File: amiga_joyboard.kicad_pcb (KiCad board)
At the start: 2 copper layers, 18 parts, among them J1 JOYPORT_OUT, SW1 FIRE_BTN, SW2 B_BTN, SW3 A_BTN, SW4 RIGHT_BTN, SW5 LEFT_BTN, SW6 DOWN_BTN, SW7 UP_BTN, SW8 AUTOFIRE_SW, SW9 AMIGA_C64_SW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

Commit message: boards separated
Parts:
- added J2: CONN_D, Connector_JST:JST_XH_S5B-XH-A_1x05_P2.50mm_Horizontal, F.Cu at (88.0, 50.5)
- added J3: CONN_F, Connector_JST:JST_XH_S5B-XH-A_1x05_P2.50mm_Horizontal, F.Cu at (173.6, 50.5)
- moved SW9 33.4 mm to (180.9, 57.2), turned to 0 degrees
- moved R1 25.2 mm to (177.8, 73.5)
- moved C2 9.86 mm to (154.9, 55.1)
- moved J1 9.36 mm to (69.5, 50.5)
- moved U1 8.39 mm to (159.3, 61.3)
- moved R3 8.27 mm to (179.1, 67.1)
- moved C1 7.84 mm to (172.7, 67.6)
- moved RV1 7.74 mm to (195.6, 67.8)
- moved R2 7.31 mm to (186.7, 63.3)
- moved D1 5.88 mm to (149.4, 59.5)
- moved SW8 5.63 mm to (145.6, 68.1)
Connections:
- C1 pad 2: GND -> GND_F
- C2 pad 2: GND -> GND_F
- J1 pad 5: /B -> /B_D
- J1 pad 6: /FIRE -> /FIRE_D
- J1 pad 7: VCC -> VCC_D
- J1 pad 8: GND -> GND_D
- J1 pad 9: /A -> /A_D
- R2 pad 2: VCC -> VCC_F
- SW1 pad 1: /FIRE -> /FIRE_F
- SW2 pad 1: /B -> /B_F
- SW3 pad 1: /A -> /A_F
- SW4 pad 2: GND -> GND_D
- SW5 pad 2: GND -> GND_D
- SW6 pad 2: GND -> GND_D
- SW7 pad 2: GND -> GND_D
- SW8 pad 2: GND -> GND_F
- SW9 pad 2: GND -> GND_F
- SW9 pad 3: VCC -> VCC_F
- U1 pad 1: GND -> GND_F
- U1 pad 4: VCC -> VCC_F
- U1 pad 8: VCC -> VCC_F

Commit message: first complete design
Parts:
- added REF**: MountingHole_M3, MountingHole:MountingHole_3.2mm_M3_ISO7380_Pad, F.Cu at (58.4, 75.4)
- added REF**: MountingHole_M3, MountingHole:MountingHole_3.2mm_M3_ISO7380_Pad, F.Cu at (121.9, 101.6)
- added REF**: MountingHole_M3, MountingHole:MountingHole_3.2mm_M3_ISO7380_Pad, F.Cu at (121.9, 75.4)
- added REF**: MountingHole_M3, MountingHole:MountingHole_3.2mm_M3_ISO7380_Pad, F.Cu at (231.1, 75.4)
- added REF**: MountingHole_M3, MountingHole:MountingHole_3.2mm_M3_ISO7380_Pad, F.Cu at (58.4, 101.6)
- added REF**: MountingHole_M3, MountingHole:MountingHole_3.2mm_M3_ISO7380_Pad, F.Cu at (170.2, 75.4)
- added REF**: MountingHole_M3, MountingHole:MountingHole_3.2mm_M3_ISO7380_Pad, F.Cu at (165.4, 101.6)
- R1: value 270 -> 100
- moved RV1 51.9 mm to (238.8, 96.4)
- moved SW2 50.1 mm to (223.8, 118.6)
- moved R3 48.3 mm to (212.3, 102.1)
- moved D1 47.6 mm to (184.4, 91.8)
- moved SW8 47.6 mm to (180.6, 100.3)
- moved R2 47.5 mm to (220.0, 97.3)
- moved R1 47.4 mm to (211.1, 107.2)
- moved C2 46.3 mm to (188.2, 87.3)
- moved SW9 46.3 mm to (214.2, 89.5)
- moved U1 46.3 mm to (192.5, 93.6)
- moved C1 46.3 mm to (206.0, 99.9)
- moved SW3 46.3 mm to (200.9, 118.6)
- moved J3 46.3 mm to (206.9, 82.8)
- moved SW1 42.8 mm to (178.1, 118.6)
- moved SW4 41.5 mm to (112.5, 118.6)
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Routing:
- net /A_F: track 0.00 -> 82.5 mm
- net /FIRE_F: track 0.00 -> 75.5 mm
- net Net-(U1-THR): track 0.00 -> 65.9 mm, vias 0 -> 2
- net /RIGHT: track 0.00 -> 57.9 mm
- net VCC_F: track 0.00 -> 57.4 mm, vias 0 -> 2
- net /B_F: track 0.00 -> 49.6 mm, vias 0 -> 2
- net Net-(R1-Pad1): track 0.00 -> 46.2 mm
- net /DOWN: track 0.00 -> 44.8 mm
- net /A_D: track 0.00 -> 43.8 mm
- net /LEFT: track 0.00 -> 42.6 mm
- net /FIRE_D: track 0.00 -> 36.1 mm, vias 0 -> 2
- net /AUTOFIRE: track 0.00 -> 34.6 mm, vias 0 -> 2
- net VCC_D: track 0.00 -> 32.3 mm, vias 0 -> 2
- net Net-(SW9-B): track 0.00 -> 31.1 mm, vias 0 -> 2
- net /B_D: track 0.00 -> 30.3 mm, vias 0 -> 2
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- added copper zone on B.Cu, net GND_D
- added copper zone on B.Cu, net GND_F
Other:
- board outline added: 192.5 x 63.5 mm

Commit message: fill tweaks
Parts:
- moved REF** 0.51 mm to (164.8, 101.6)
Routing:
- net GND_D: track 25.3 -> 60.3 mm
- net GND_F: track 22.6 -> 25.9 mm
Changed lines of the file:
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@@
 	(footprint "MountingHole:MountingHole_3.2mm_M3_ISO7380_Pad"
 		(layer "F.Cu")
-		(at 165.354 101.6)
+		(at 164.846 101.6)
 		(descr "Mounting Hole 3.2mm, M3, ISO7380")
 		(tags "mounting hole 3.2mm m3 iso7380")
@@
 	)
 	(segment
+		(start 215.138 91.52)
+		(end 215.138 91.948)
+		(width 1)
+		(layer "B.Cu")
+		(net 2)
+	)
+	(segment
 		(start 190.221113 82.804)
 		(end 196.89 82.804)
@@
 	)
 	(segment
+		(start 217.17 89.488)
+		(end 215.138 91.52)
+		(width 1)
+		(layer "B.Cu")
+		(net 2)
+	)
+	(segment
 		(start 189.738 91.44)
 		(end 189.738 95.452)
@@
 	)
 	(segment
+		(start 94.343497 71.229497)
+		(end 94.343497 73.261497)
+		(width 1)
+		(layer "B.Cu")
+		(net 9)
+	)
+	(segment
 		(start 108.712 116.078)
 		(end 106.934 114.3)
@@
 	)
 	(segment
+		(start 79.077 69.98)
+		(end 93.094 69.98)
+		(width 1)
+		(layer "B.Cu")
+		(net 9)
+	)
+	(segment
+		(start 73.058 77.724)
+		(end 73.058 75.999)
+		(width 1)
+		(layer "B.Cu")
+		(net 9)
+	)
+	(segment
+		(start 95.758 74.676)
+		(end 95.758 74.93)
+		(width 1)
+		(layer "B.Cu")
+		(net 9)
+	)
+	(segment
+		(start 73.058 77.724)
+		(end 73.058 80.17)
+		(width 1)
+		(layer "B.Cu")
+		(net 9)
+	)
+	(segment
 		(start 82.55 104.648)
 		(end 82.826675 104.924675)
@@
 	)
 	(segment
+		(start 99.06 77.724)
+		(end 96.774 77.724)
+		(width 1)
+		(layer "B.Cu")
+		(net 9)
+	)
+	(segment
+		(start 93.094 69.98)
+		(end 93.472 70.358)
+		(width 1)
+		(layer "B.Cu")
+		(net 9)
+	)
+	(segment
 		(start 62.992 116.078)
 		(end 60.96 114.046)
+		(width 1)
+		(layer "B.Cu")
+		(net 9)
+	)
+	(segment
+		(start 93.472 70.358)
+		(end 94.343497 71.229497)
+		(width 1)
+		(layer "B.Cu")
+		(net 9)
+	)
+	(segment
+		(start 94.343497 73.261497)
+		(end 94.996 73.914)
+		(width 1)
+		(layer "B.Cu")
+		(net 9)
+	)
+	(segment
+		(start 94.996 73.914)
+		(end 95.758 74.676)
+		(width 1)
+		(layer "B.Cu")
+		(net 9)
+	)
+	(segment
+		(start 73.058 75.999)
+		(end 79.077 69.98)
 		(width 1)
 		(layer "B.Cu")
@@
 		(priority 1)
 		(connect_pads
-			(clearance 0.5)
-		)
-		(min_thickness 0.25)
+			(clearance 1)
+		)
+		(min_thickness 0.7)
 		(filled_areas_thickness no)
 		(fill yes
-			(thermal_gap 0.5)
-			(thermal_bridge_width 0.5)
+			(thermal_gap 0.7)
+			(thermal_bridge_width 0.7)
 			(smoothing fillet)
-			(radius 0.5)
+			(radius 2)
 		)
 		(polygon
@@
 		(hatch edge 0.5)
 		(connect_pads
-			(clearance 0.5)
-		)
-		(min_thickness 0.25)
+			(clearance 1)
+		)
+		(min_thickness 0.7)
 		(filled_areas_thickness no)
 		(fill yes
-			(thermal_gap 0.5)
-			(thermal_bridge_width 0.5)
+			(thermal_gap 0.7)
+			(thermal_bridge_width 0.7)
 			(smoothing fillet)
-			(radius 0.5)
+			(radius 2)
 		)
 		(polygon

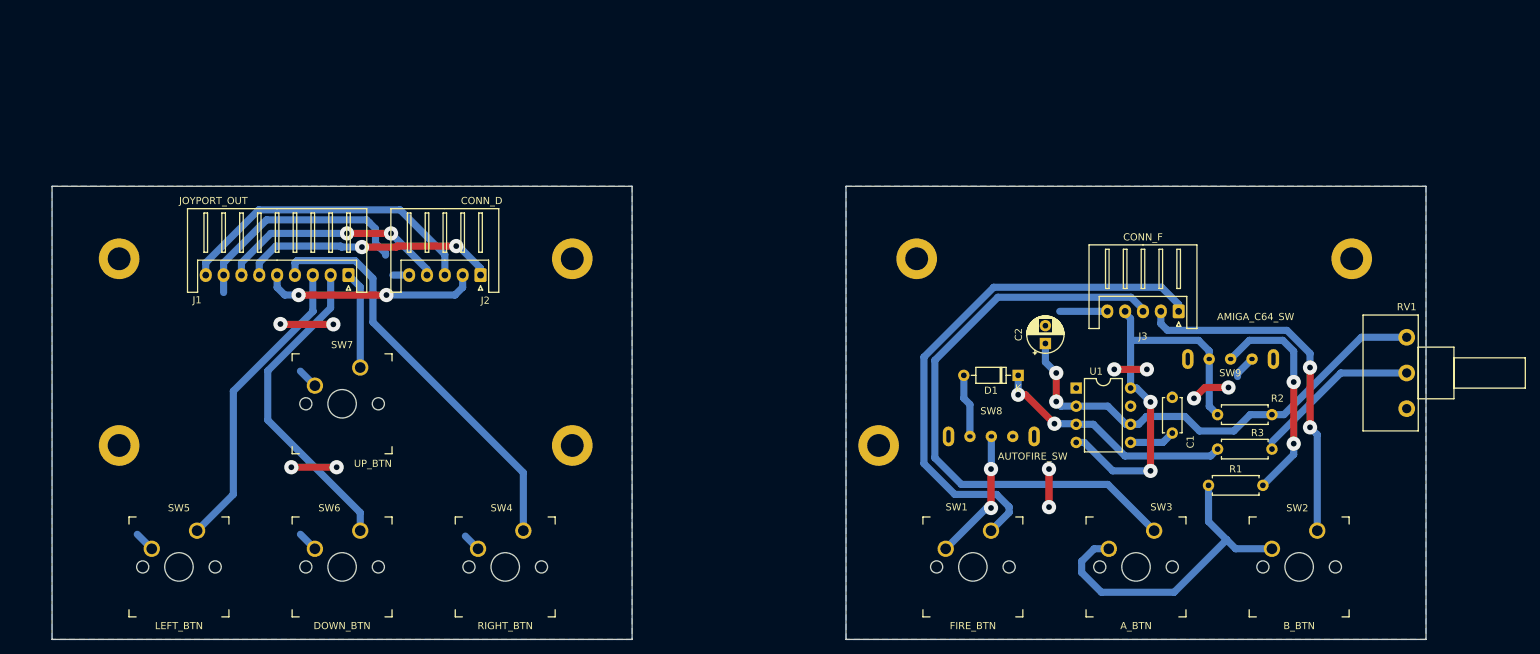
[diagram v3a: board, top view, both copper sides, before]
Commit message: m3 mounting holes swapped for m5 holes (to accommodate a post with m3 screw going through)
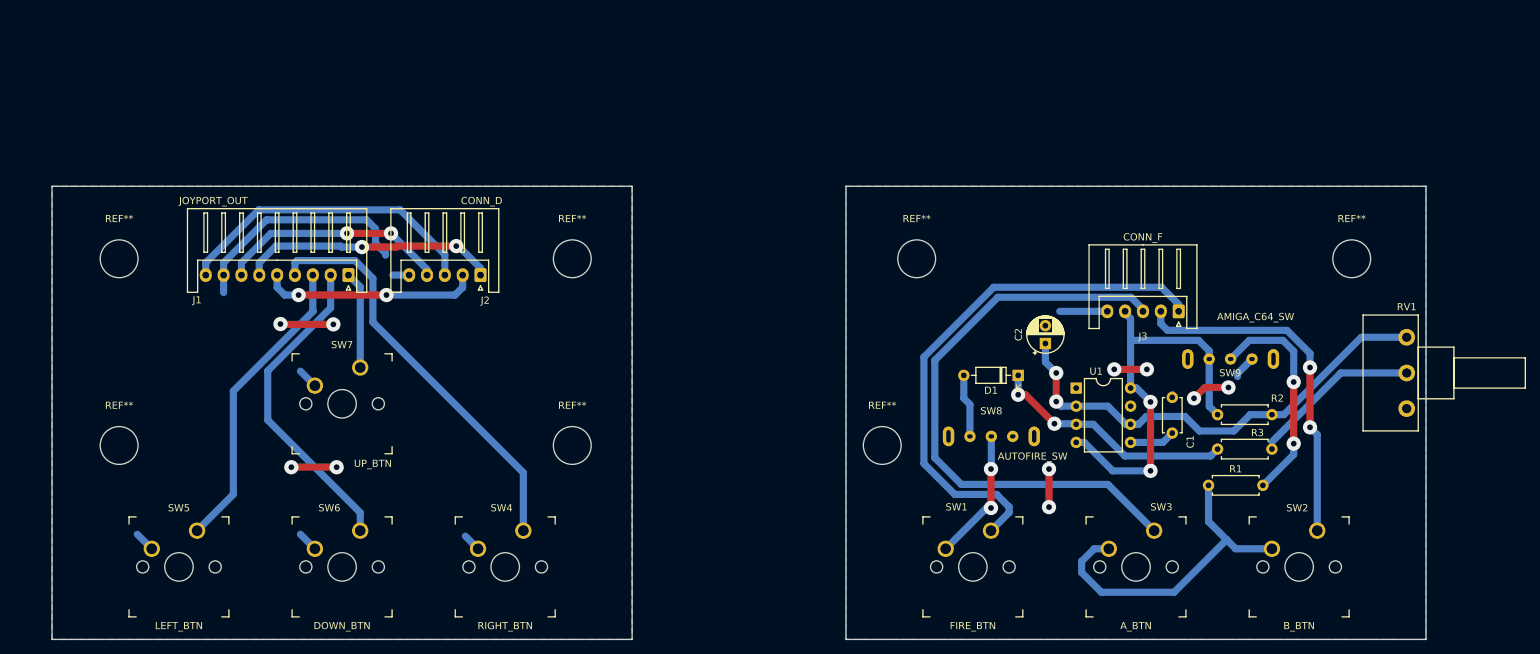
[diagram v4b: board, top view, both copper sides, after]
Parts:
- REF** (x7): footprint MountingHole:MountingHole_3.2mm_M3_ISO7380_Pad -> MountingHole:MountingHole_5.3mm_M5_DIN965
- moved REF** 0.51 mm to (165.4, 101.6)
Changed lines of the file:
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@@
 		)
 	)
-	(footprint "MountingHole:MountingHole_3.2mm_M3_ISO7380_Pad"
+	(footprint "MountingHole:MountingHole_5.3mm_M5_DIN965"
 		(layer "F.Cu")
 		(at 58.42 75.438)
-		(descr "Mounting Hole 3.2mm, M3, ISO7380")
-		(tags "mounting hole 3.2mm m3 iso7380")
+		(descr "Mounting Hole 5.3mm, no annular, M5, DIN965")
+		(tags "mounting hole 5.3mm no annular m5 din965")
 		(property "Reference" "REF**"
-			(at 0 -3.85 0)
+			(at 0 -5.6 0)
 			(layer "F.SilkS")
-			(hide yes)
 			(effects
 				(font
@@
 		)
 		(property "Value" "MountingHole_M3"
-			(at 2.54 4.064 0)
+			(at 0 5.6 0)
 			(layer "F.Fab")
 			(hide yes)
@@
 			)
 		)
-		(property "Footprint" "MountingHole:MountingHole_3.2mm_M3_ISO7380_Pad"
+		(property "Footprint" "MountingHole:MountingHole_5.3mm_M5_DIN965"
 			(at 0 0 0)
 			(unlocked yes)
@@
 			)
 		)
-		(attr board_only exclude_from_pos_files exclude_from_bom)
+		(attr exclude_from_pos_files exclude_from_bom)
 		(fp_circle
 			(center 0 0)
-			(end 2.85 0)
+			(end 4.6 0)
 			(stroke
 				(width 0.15)
@@
 		(fp_circle
 			(center 0 0)
-			(end 3.1 0)
+			(end 4.85 0)
 			(stroke
 				(width 0.05)
@@
 			)
 		)
-		(pad "1" thru_hole circle
+		(pad "" np_thru_hole circle
 			(at 0 0)
-			(size 5.7 5.7)
-			(drill 3.2)
+			(size 5.3 5.3)
+			(drill 5.3)
 			(layers "*.Cu" "*.Mask")
-			(remove_unused_layers no)
 		)
 	)
-	(footprint "MountingHole:MountingHole_3.2mm_M3_ISO7380_Pad"
+	(footprint "MountingHole:MountingHole_5.3mm_M5_DIN965"
 		(layer "F.Cu")
 		(at 121.92 101.6)
-		(descr "Mounting Hole 3.2mm, M3, ISO7380")
-		(tags "mounting hole 3.2mm m3 iso7380")
+		(descr "Mounting Hole 5.3mm, no annular, M5, DIN965")
+		(tags "mounting hole 5.3mm no annular m5 din965")
 		(property "Reference" "REF**"
-			(at 0 -3.85 0)
+			(at 0 -5.6 0)
 			(layer "F.SilkS")
-			(hide yes)
 			(effects
 				(font
@@
 		)
 		(property "Value" "MountingHole_M3"
-			(at 0 3.85 0)
+			(at 0 5.6 0)
 			(layer "F.Fab")
 			(hide yes)
@@
 			)
 		)
-		(property "Footprint" "MountingHole:MountingHole_3.2mm_M3_ISO7380_Pad"
+		(property "Footprint" "MountingHole:MountingHole_5.3mm_M5_DIN965"
 			(at 0 0 0)
 			(unlocked yes)
@@
 			)
 		)
-		(attr board_only exclude_from_pos_files exclude_from_bom)
+		(attr exclude_from_pos_files exclude_from_bom)
 		(fp_circle
 			(center 0 0)
-			(end 2.85 0)
+			(end 4.6 0)
 			(stroke
 				(width 0.15)
@@
 		(fp_circle
 			(center 0 0)
-			(end 3.1 0)
+			(end 4.85 0)
 			(stroke
 				(width 0.05)
@@
 			)
 		)
-		(pad "1" thru_hole circle
+		(pad "" np_thru_hole circle
 			(at 0 0)
-			(size 5.7 5.7)
-			(drill 3.2)
+			(size 5.3 5.3)
+			(drill 5.3)
 			(layers "*.Cu" "*.Mask")
-			(remove_unused_layers no)
 		)
 	)
@@
 		)
 	)
-	(footprint "MountingHole:MountingHole_3.2mm_M3_ISO7380_Pad"
+	(footprint "MountingHole:MountingHole_5.3mm_M5_DIN965"
 		(layer "F.Cu")
 		(at 121.92 75.438)
-		(descr "Mounting Hole 3.2mm, M3, ISO7380")
-		(tags "mounting hole 3.2mm m3 iso7380")
+		(descr "Mounting Hole 5.3mm, no annular, M5, DIN965")
+		(tags "mounting hole 5.3mm no annular m5 din965")
 		(property "Reference" "REF**"
-			(at 0 -3.85 0)
+			(at 0 -5.6 0)
 			(layer "F.SilkS")
-			(hide yes)
 			(effects
 				(font
@@
 		)
 		(property "Value" "MountingHole_M3"
-			(at 0 3.85 0)
+			(at 0 5.6 0)
 			(layer "F.Fab")
 			(hide yes)
@@
 			)
 		)
-		(property "Footprint" "MountingHole:MountingHole_3.2mm_M3_ISO7380_Pad"
+		(property "Footprint" "MountingHole:MountingHole_5.3mm_M5_DIN965"
 			(at 0 0 0)
 			(unlocked yes)
@@
 			)
 		)
-		(attr board_only exclude_from_pos_files exclude_from_bom)
+		(attr exclude_from_pos_files exclude_from_bom)
 		(fp_circle
 			(center 0 0)
-			(end 2.85 0)
+			(end 4.6 0)
 			(stroke
 				(width 0.15)
@@
 		(fp_circle
 			(center 0 0)
-			(end 3.1 0)
+			(end 4.85 0)
 			(stroke
 				(width 0.05)
@@
 			)
 		)
-		(pad "1" thru_hole circle
+		(pad "" np_thru_hole circle
 			(at 0 0)
-			(size 5.7 5.7)
-			(drill 3.2)
+			(size 5.3 5.3)
+			(drill 5.3)
 			(layers "*.Cu" "*.Mask")
-			(remove_unused_layers no)
 		)
 	)
@@
 		)
 	)
-	(footprint "MountingHole:MountingHole_3.2mm_M3_ISO7380_Pad"
+	(footprint "MountingHole:MountingHole_5.3mm_M5_DIN965"
 		(layer "F.Cu")
 		(at 231.14 75.438)
-		(descr "Mounting Hole 3.2mm, M3, ISO7380")
-		(tags "mounting hole 3.2mm m3 iso7380")
+		(descr "Mounting Hole 5.3mm, no annular, M5, DIN965")
+		(tags "mounting hole 5.3mm no annular m5 din965")
 		(property "Reference" "REF**"
-			(at 0 -3.85 0)
+			(at 0 -5.6 0)
 			(layer "F.SilkS")
-			(hide yes)
 			(effects
 				(font
@@
 		)
 		(property "Value" "MountingHole_M3"
-			(at 0 3.85 0)
+			(at 0 5.6 0)
 			(layer "F.Fab")
 			(hide yes)
@@
 			)
 		)
-		(property "Footprint" "MountingHole:MountingHole_3.2mm_M3_ISO7380_Pad"
+		(property "Footprint" "MountingHole:MountingHole_5.3mm_M5_DIN965"
 			(at 0 0 0)
 			(unlocked yes)
@@
 			)
 		)
-		(attr board_only exclude_from_pos_files exclude_from_bom)
+		(attr exclude_from_pos_files exclude_from_bom)
 		(fp_circle
 			(center 0 0)
-			(end 2.85 0)
+			(end 4.6 0)
 			(stroke
 				(width 0.15)
@@
 		(fp_circle
 			(center 0 0)
-			(end 3.1 0)
+			(end 4.85 0)
 			(stroke
 				(width 0.05)
@@
 			)
 		)
-		(pad "1" thru_hole circle
+		(pad "" np_thru_hole circle
 			(at 0 0)
-			(size 5.7 5.7)
-			(drill 3.2)
+			(size 5.3 5.3)
+			(drill 5.3)
 			(layers "*.Cu" "*.Mask")
-			(remove_unused_layers no)
 		)
 	)
@@
 		)
 	)
-	(footprint "MountingHole:MountingHole_3.2mm_M3_ISO7380_Pad"
+	(footprint "MountingHole:MountingHole_5.3mm_M5_DIN965"
 		(layer "F.Cu")
 		(at 58.42 101.6)
-		(descr "Mounting Hole 3.2mm, M3, ISO7380")
-		(tags "mounting hole 3.2mm m3 iso7380")
+		(descr "Mounting Hole 5.3mm, no annular, M5, DIN965")
+		(tags "mounting hole 5.3mm no annular m5 din965")
 		(property "Reference" "REF**"
-			(at 0 -3.85 0)
+			(at 0 -5.6 0)
 			(layer "F.SilkS")
-			(hide yes)
 			(effects
 				(font
@@
 		)
 		(property "Value" "MountingHole_M3"
-			(at 0 3.85 0)
+			(at 0 5.6 0)
 			(layer "F.Fab")
 			(hide yes)
@@
 			)
 		)
-		(property "Footprint" "MountingHole:MountingHole_3.2mm_M3_ISO7380_Pad"
+		(property "Footprint" "MountingHole:MountingHole_5.3mm_M5_DIN965"
 			(at 0 0 0)
 			(unlocked yes)
@@
 			)
 		)
-		(attr board_only exclude_from_pos_files exclude_from_bom)
+		(attr exclude_from_pos_files exclude_from_bom)
 		(fp_circle
 			(center 0 0)
-			(end 2.85 0)
+			(end 4.6 0)
 			(stroke
 				(width 0.15)
@@
 		(fp_circle
 			(center 0 0)
-			(end 3.1 0)
+			(end 4.85 0)
 			(stroke
 				(width 0.05)
@@
 			)
 		)
-		(pad "1" thru_hole circle
+		(pad "" np_thru_hole circle
 			(at 0 0)
-			(size 5.7 5.7)
-			(drill 3.2)
+			(size 5.3 5.3)
+			(drill 5.3)
 			(layers "*.Cu" "*.Mask")
-			(remove_unused_layers no)
 		)
 	)
@@
 		)
 	)
-	(footprint "MountingHole:MountingHole_3.2mm_M3_ISO7380_Pad"
+	(footprint "MountingHole:MountingHole_5.3mm_M5_DIN965"
 		(layer "F.Cu")
 		(at 170.18 75.438)
-		(descr "Mounting Hole 3.2mm, M3, ISO7380")
-		(tags "mounting hole 3.2mm m3 iso7380")
+		(descr "Mounting Hole 5.3mm, no annular, M5, DIN965")
+		(tags "mounting hole 5.3mm no annular m5 din965")
 		(property "Reference" "REF**"
-			(at 0 -3.85 0)
+			(at 0 -5.6 0)
 			(layer "F.SilkS")
-			(hide yes)
 			(effects
 				(font
@@
 		)
 		(property "Value" "MountingHole_M3"
-			(at 0 3.85 0)
+			(at 0 5.6 0)
 			(layer "F.Fab")
 			(hide yes)
@@
 			)
 		)
-		(property "Footprint" "MountingHole:MountingHole_3.2mm_M3_ISO7380_Pad"
+		(property "Footprint" "MountingHole:MountingHole_5.3mm_M5_DIN965"
 			(at 0 0 0)
 			(unlocked yes)
@@
 			)
 		)
-		(attr board_only exclude_from_pos_files exclude_from_bom)
+		(attr exclude_from_pos_files exclude_from_bom)
 		(fp_circle
 			(center 0 0)
-			(end 2.85 0)
+			(end 4.6 0)
 			(stroke
 				(width 0.15)
@@
 		(fp_circle
 			(center 0 0)
-			(end 3.1 0)
+			(end 4.85 0)
 			(stroke
 				(width 0.05)
@@
 			)
 		)
-		(pad "1" thru_hole circle
+		(pad "" np_thru_hole circle
 			(at 0 0)
-			(size 5.7 5.7)
-			(drill 3.2)
+			(size 5.3 5.3)
+			(drill 5.3)
 			(layers "*.Cu" "*.Mask")
-			(remove_unused_layers no)
 		)
 	)
@@
 		)
 	)
-	(footprint "MountingHole:MountingHole_3.2mm_M3_ISO7380_Pad"
+	(footprint "MountingHole:MountingHole_5.3mm_M5_DIN965"
 		(layer "F.Cu")
-		(at 164.846 101.6)
-		(descr "Mounting Hole 3.2mm, M3, ISO7380")
-		(tags "mounting hole 3.2mm m3 iso7380")
+		(at 165.354 101.6)
+		(descr "Mounting Hole 5.3mm, no annular, M5, DIN965")
+		(tags "mounting hole 5.3mm no annular m5 din965")
 		(property "Reference" "REF**"
-			(at 0 -3.85 0)
+			(at 0 -5.6 0)
 			(layer "F.SilkS")
-			(hide yes)
 			(effects
 				(font
@@
 		)
 		(property "Value" "MountingHole_M3"
-			(at 0 3.85 0)
+			(at 0 5.6 0)
 			(layer "F.Fab")
 			(hide yes)
@@
 			)
 		)
-		(property "Footprint" "MountingHole:MountingHole_3.2mm_M3_ISO7380_Pad"
+		(property "Footprint" "MountingHole:MountingHole_5.3mm_M5_DIN965"
 			(at 0 0 0)
 			(unlocked yes)
@@
 			)
 		)
-		(attr board_only exclude_from_pos_files exclude_from_bom)
+		(attr exclude_from_pos_files exclude_from_bom)
 		(fp_circle
 			(center 0 0)
-			(end 2.85 0)
+			(end 4.6 0)
 			(stroke
 				(width 0.15)
@@
 		(fp_circle
 			(center 0 0)
-			(end 3.1 0)
+			(end 4.85 0)
 			(stroke
 				(width 0.05)
@@
 			)
 		)
-		(pad "1" thru_hole circle
+		(pad "" np_thru_hole circle
 			(at 0 0)
-			(size 5.7 5.7)
-			(drill 3.2)
+			(size 5.3 5.3)
+			(drill 5.3)
 			(layers "*.Cu" "*.Mask")
-			(remove_unused_layers no)
 		)
 	)
